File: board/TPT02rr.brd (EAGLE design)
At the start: 28.2 x 28.2 mm, 16 parts, among them SW4 SW_SLIDECUS12B, U1 MOD_CYBLE014008-00, U2 REG_TPS61221

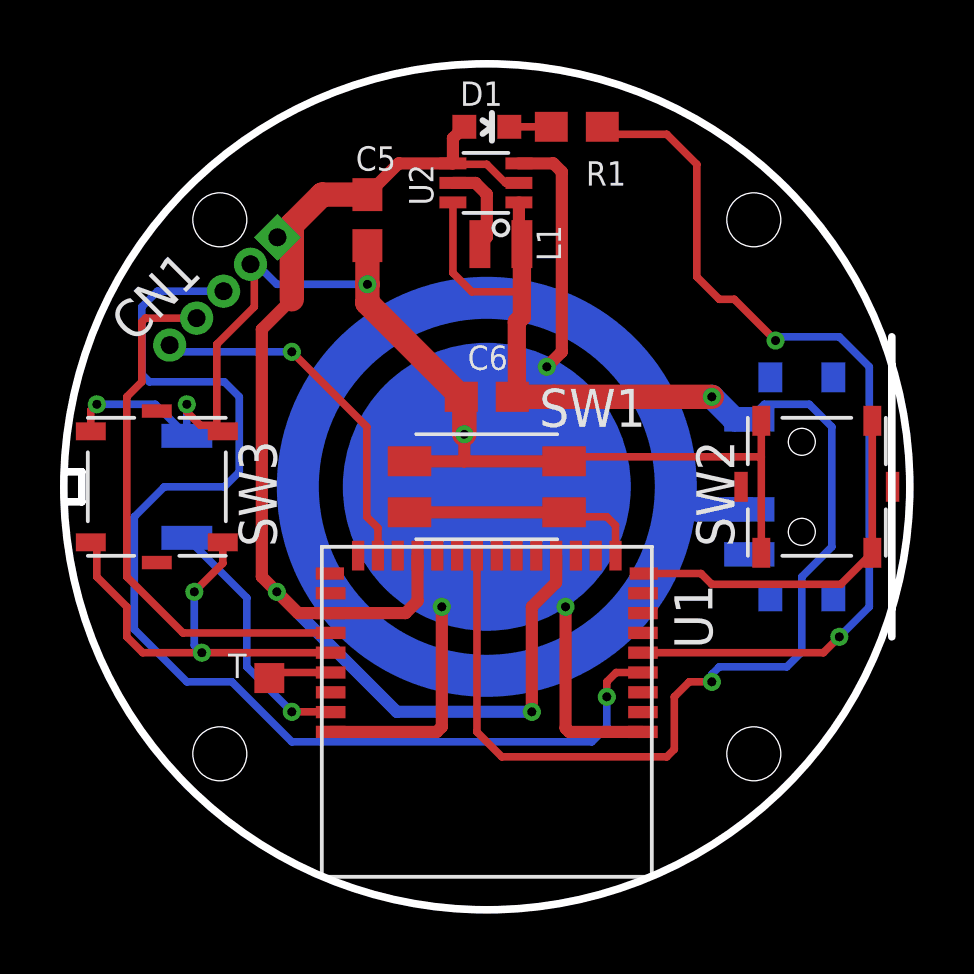
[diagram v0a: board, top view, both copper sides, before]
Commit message: Cの部品番号を整理。Elecrow向けBOMを作成。
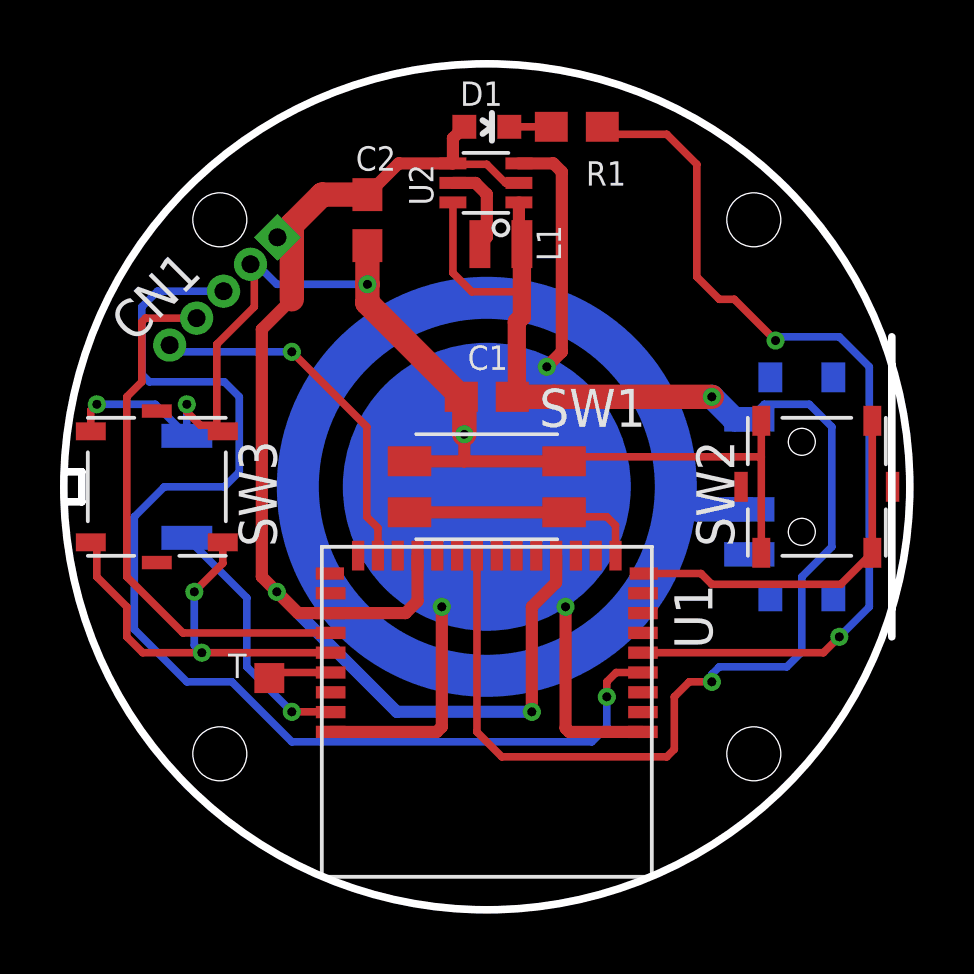
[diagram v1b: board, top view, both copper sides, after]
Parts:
- renumbered C5 to C2, C6 to C1
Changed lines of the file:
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@@
 <?xml version="1.0" encoding="utf-8"?>
 <!DOCTYPE eagle SYSTEM "eagle.dtd">
-<eagle version="7.5.0">
+<eagle version="7.7.0">
 <drawing>
 <settings>
@@
 <setting verticaltext="up"/>
 </settings>
-<grid distance="1" unitdist="mm" unit="mm" style="lines" multiple="1" display="yes" altdistance="0.25" altunitdist="mm" altunit="mm"/>
+<grid distance="1.27" unitdist="mm" unit="mm" style="lines" multiple="1" display="yes" altdistance="0.25" altunitdist="mm" altunit="mm"/>
 <layers>
 <layer number="1" name="Top" color="4" fill="1" visible="no" active="yes"/>
@@
 </autorouter>
 <elements>
-<element name="C5" library="akita" package="0603" value="10u" x="11.02" y="23.89" smashed="yes" rot="R270">
+<element name="C2" library="akita" package="0603" value="10u" x="11.02" y="23.89" smashed="yes" rot="R270">
 <attribute name="NAME" x="10.631" y="25.537" size="0.8128" layer="25" font="vector"/>
 <attribute name="VALUE" x="9.242" y="24.906" size="0.8128" layer="27" font="vector" rot="R270"/>
 </element>
-<element name="C6" library="akita" package="0603" value="10u" x="15" y="18" smashed="yes" rot="R180">
+<element name="C1" library="akita" package="0603" value="10u" x="15" y="18" smashed="yes" rot="R180">
 <attribute name="NAME" x="14.361" y="18.897" size="0.8128" layer="25" font="vector"/>
 <attribute name="VALUE" x="16.016" y="19.778" size="0.8128" layer="27" font="vector" rot="R180"/>
@@
 <signal name="GND">
 <contactref element="CN1" pad="P$2"/>
-<contactref element="C5" pad="2"/>
-<contactref element="C6" pad="2"/>
+<contactref element="C2" pad="2"/>
+<contactref element="C1" pad="2"/>
 <contactref element="CNM" pad="P$1"/>
 <contactref element="SW3" pad="B2"/>
@@
 <via x="8" y="11.5" extent="1-16" drill="0.3"/>
 <contactref element="U2" pad="P$4"/>
-<contactref element="C5" pad="1"/>
+<contactref element="C2" pad="1"/>
 <contactref element="U2" pad="P$2"/>
 <wire x1="11.02" y1="24.74" x2="9.51" y2="24.74" width="0.8128" layer="1"/>
@@
 </signal>
 <signal name="VBAT">
-<contactref element="C6" pad="1"/>
+<contactref element="C1" pad="1"/>
 <contactref element="SW4" pad="P$1"/>
 <via x="22.5" y="18" extent="1-16" drill="0.3"/>
